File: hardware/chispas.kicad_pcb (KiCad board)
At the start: 2 copper layers, 90 x 60 mm, 41 parts, among them J1 Conn_01x05, J2 Conn_01x04, J3 Conn_01x04, J4 Conn_01x06, J5 Conn_01x02, J6 TRAFO, U1 Heltec_WiFi_LoRa_32_V3, U2 PC817X2CSP9F, U3 PAM8302AASCR

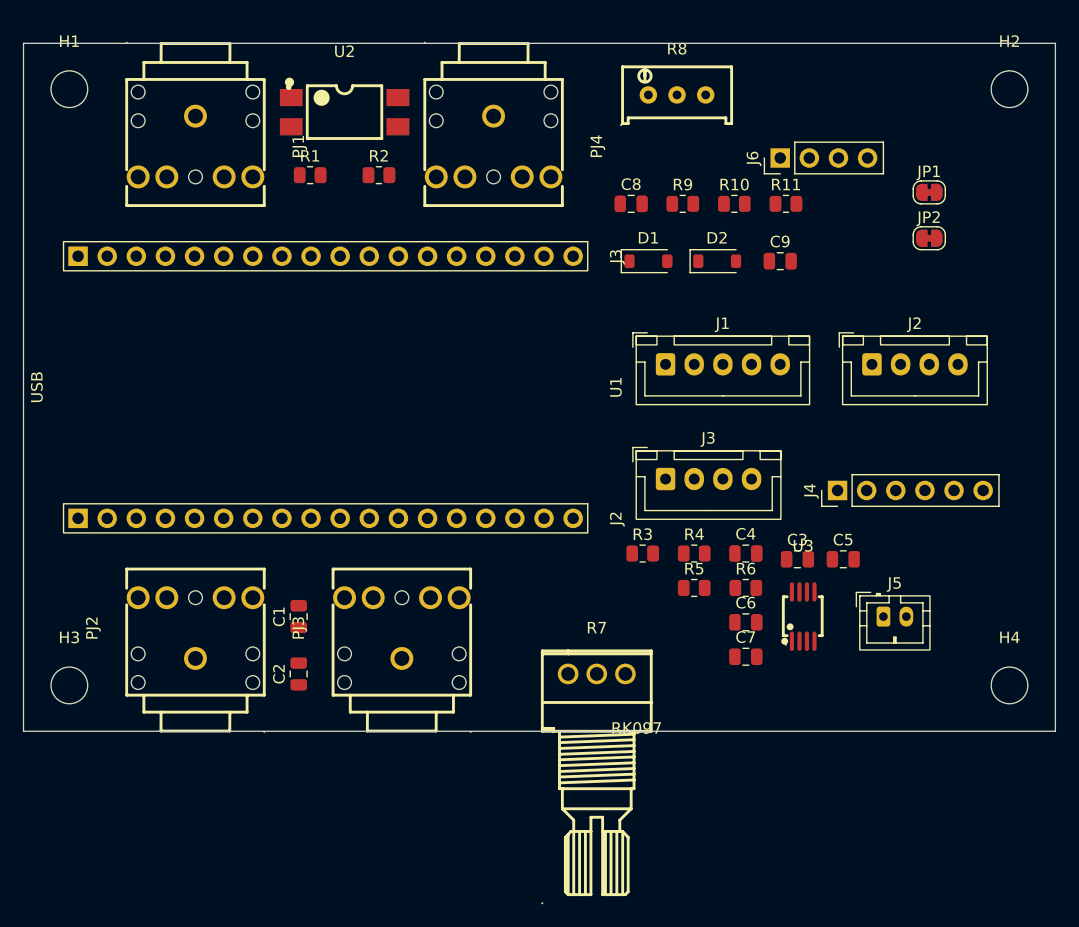
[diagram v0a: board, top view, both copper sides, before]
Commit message: PCB: encoder U4 junto a la Heltec con sus filtros; BME280 y GPS al borde derecho; tira de pines delante
Co-Authored-By: Claude Opus 5.5 <noreply@anthropic.com>
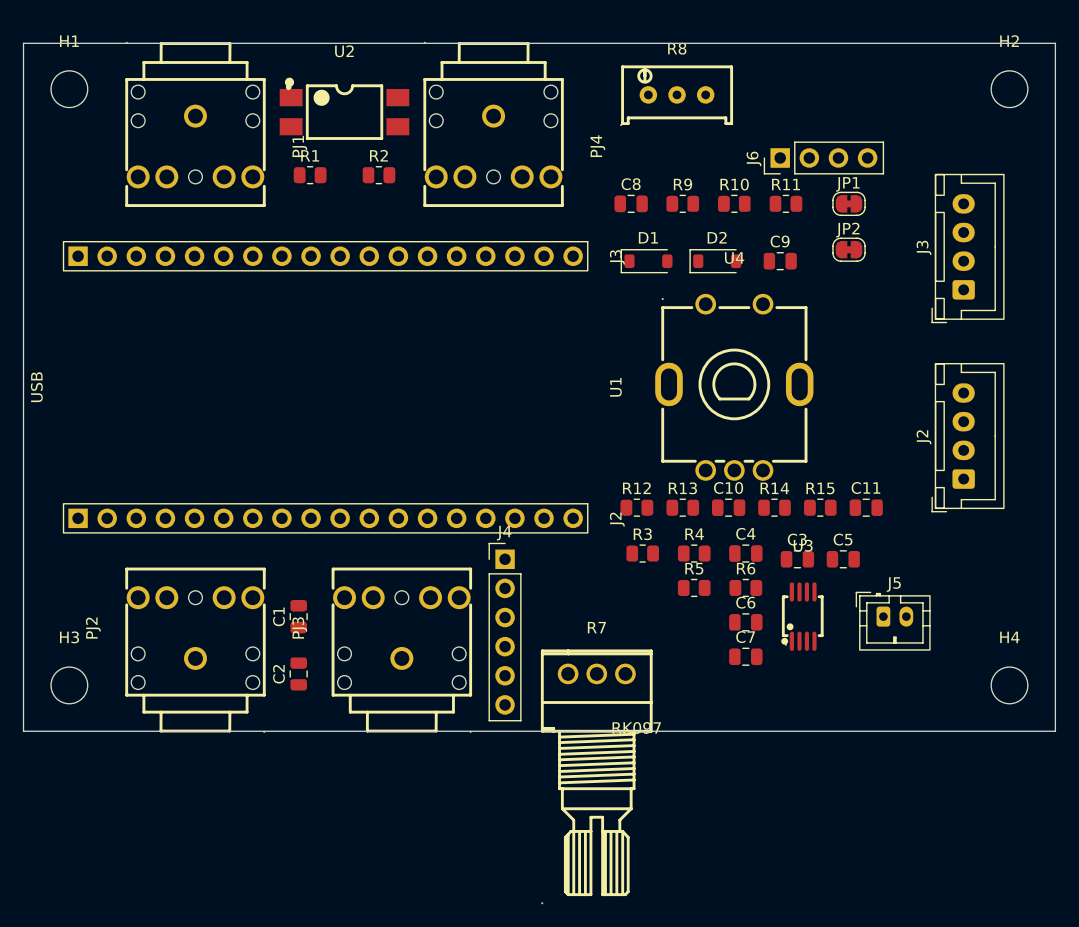
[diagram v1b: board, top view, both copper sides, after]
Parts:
- removed J1: Conn_01x05, Connector_JST:JST_XH_B5B-XH-A_1x05_P2.50mm_Vertical
- added C10: 10n, Capacitor_SMD:C_0805_2012Metric, F.Cu at (161.5, 140.5)
- added C11: 10n, Capacitor_SMD:C_0805_2012Metric, F.Cu at (173.5, 140.5)
- added R12: 10K, Resistor_SMD:R_0805_2012Metric, F.Cu at (153.5, 140.5)
- added R13: 10K, Resistor_SMD:R_0805_2012Metric, F.Cu at (157.5, 140.5)
- added R14: 10K, Resistor_SMD:R_0805_2012Metric, F.Cu at (165.5, 140.5)
- added R15: 10K, Resistor_SMD:R_0805_2012Metric, F.Cu at (169.5, 140.5)
- added U4: PEC11R-4230F-S0024, chispas:SW-TH_PEC11R-4XXXF-SXXXX, F.Cu at (162.0, 130.0)
- moved J3 30.8 mm to (182.0, 121.5), turned to 90 degrees
- moved J4 29.6 mm to (142.0, 145.0), turned to 0 degrees
- moved J2 12.8 mm to (182.0, 138.0), turned to 90 degrees
- moved JP1 7.07 mm to (172.0, 114.0)
- moved JP2 7.07 mm to (172.0, 118.0)

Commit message: PCB: jacks con el cañon asomando 1,65 mm; NOTAS: encoder en placa y requisitos de la caja
Co-Authored-By: Claude Opus 5.5 <noreply@anthropic.com>
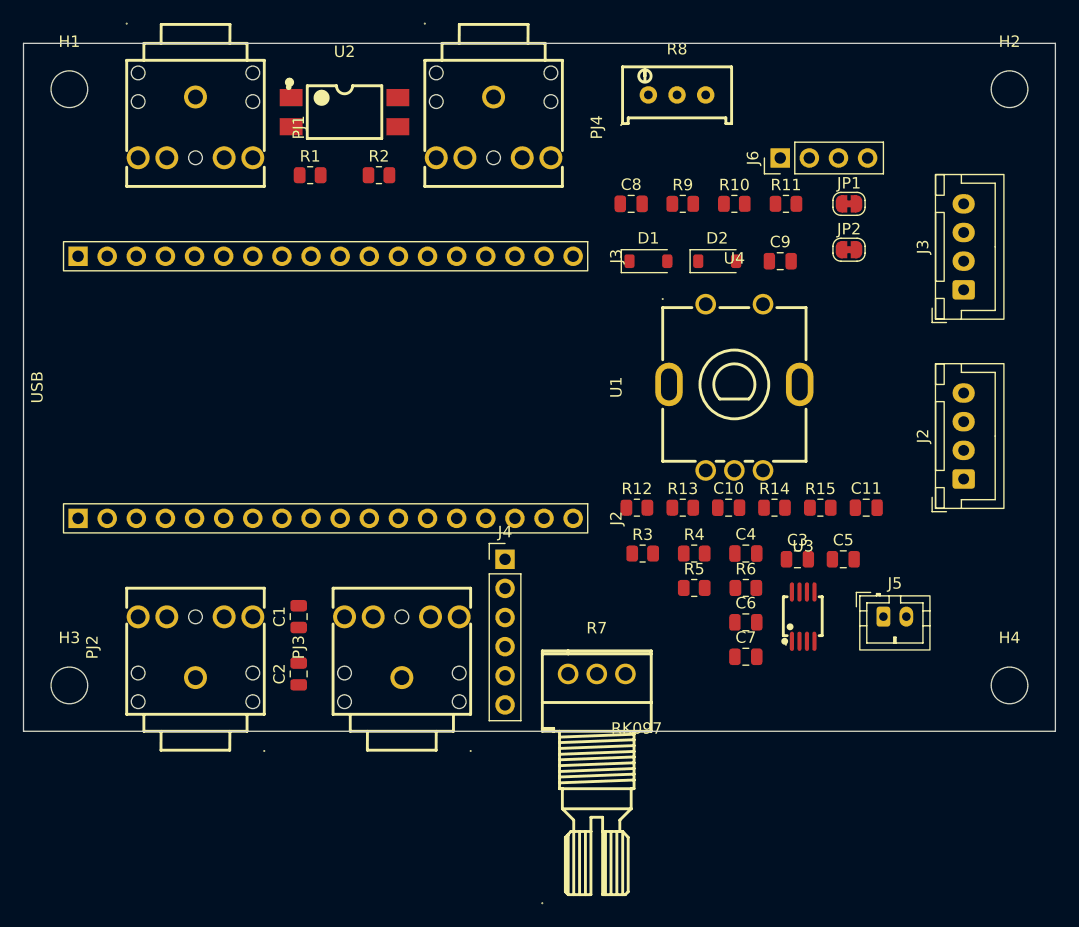
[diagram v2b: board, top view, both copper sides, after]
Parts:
- moved PJ1 1.67 mm to (115.0, 107.3)
- moved PJ4 1.67 mm to (141.0, 107.3)
- moved PJ2 1.67 mm to (115.0, 152.7)
- moved PJ3 1.67 mm to (133.0, 152.7)
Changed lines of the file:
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@@
 	(footprint "chispas:AUDIO-TH_PJ-307"
 		(layer "F.Cu")
-		(at 133 151 90)
+		(at 133 152.67 90)
 		(property "Reference" "PJ3"
 			(at 0 -9 90)
@@
 	(footprint "chispas:AUDIO-TH_PJ-307"
 		(layer "F.Cu")
-		(at 115 109 -90)
+		(at 115 107.33 -90)
 		(property "Reference" "PJ1"
 			(at 0 -9 270)
@@
 	(footprint "chispas:AUDIO-TH_PJ-307"
 		(layer "F.Cu")
-		(at 141 109 -90)
+		(at 141 107.33 -90)
 		(property "Reference" "PJ4"
 			(at 0 -9 270)
@@
 	(footprint "chispas:AUDIO-TH_PJ-307"
 		(layer "F.Cu")
-		(at 115 151 90)
+		(at 115 152.67 90)
 		(property "Reference" "PJ2"
 			(at 0 -9 90)

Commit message: PCB: placa rutada con Freerouting, planos de masa en las dos caras, 116 vias de cosido y zona aislada del KEY (DRC: 0 sin conectar, solo serigrafia)
Co-Authored-By: Claude Opus 5.5 <noreply@anthropic.com>
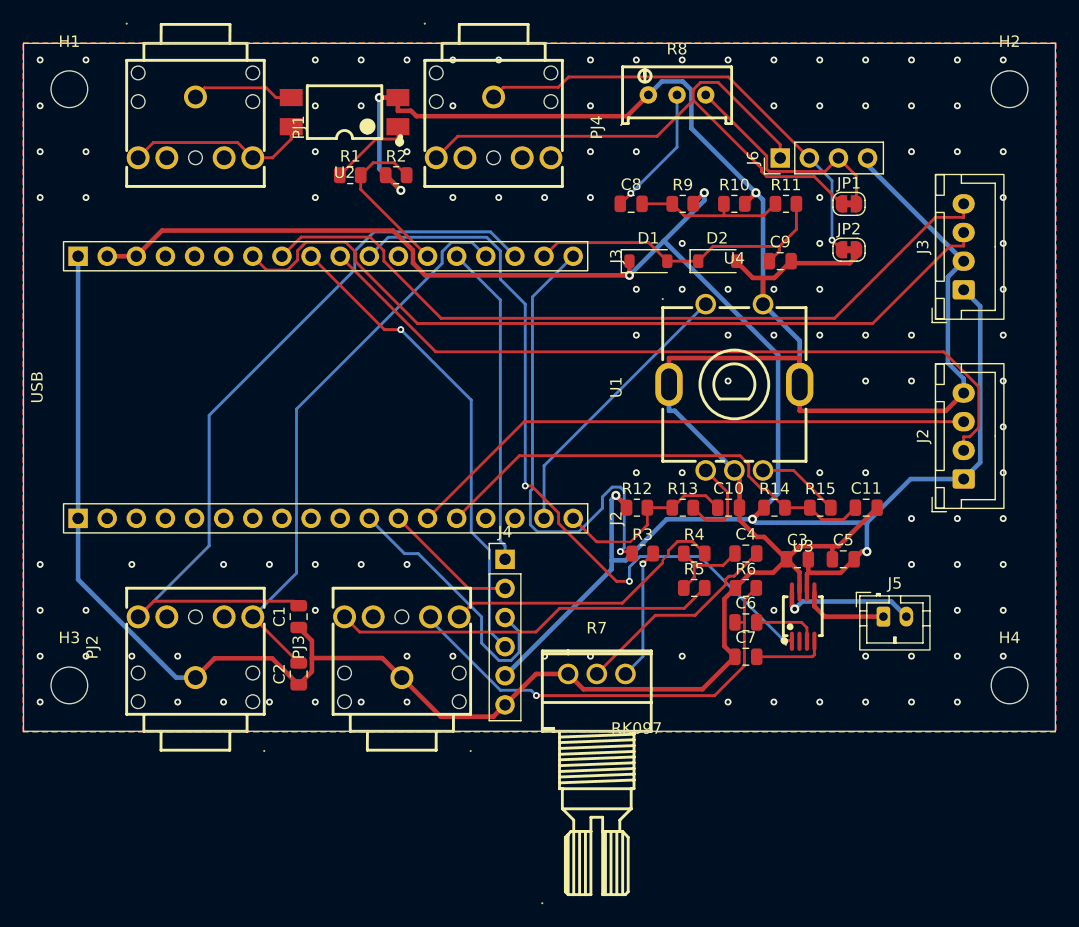
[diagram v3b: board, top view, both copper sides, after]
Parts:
- moved R1 3.50 mm to (128.5, 111.5)
- moved R2 1.50 mm to (132.5, 111.5)
- turned U2 to 180 degrees
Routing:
- net GND: track 0.00 -> 292.6 mm, vias 0 -> 119
- net +3.3V: track 0.00 -> 176.1 mm, vias 0 -> 5
- net /SCL: track 0.00 -> 71.4 mm
- net /DAH: track 0.00 -> 70.0 mm
- net /SDA: track 0.00 -> 68.4 mm
- net /GPS_RX: track 0.00 -> 66.8 mm
- net /AMP_SD: track 0.00 -> 65.9 mm, vias 0 -> 3
- net /TJ: track 0.00 -> 53.5 mm
- net /GPS_TX: track 0.00 -> 50.3 mm
- net /DIT: track 0.00 -> 49.0 mm
- net /TONO: track 0.00 -> 42.3 mm, vias 0 -> 1
- net /GPIO40: track 0.00 -> 41.9 mm, vias 0 -> 1
- net /ENC_DT: track 0.00 -> 40.4 mm
- net /SJ: track 0.00 -> 40.4 mm, vias 0 -> 1
- net /TN: track 0.00 -> 39.5 mm, vias 0 -> 1
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- added copper zone on B.Cu, net GND
- added copper zone on F.Cu, net GND

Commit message: PCB: serigrafia (nombres de conectores, nota del trafo, AUX; datos, licencia y JLCJLCJLCJLC por detras) con serigrafia.py
Co-Authored-By: Claude Opus 5.5 <noreply@anthropic.com>
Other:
- board text added: "ALTAVOZ"
- board text added: "AURIC."
- board text added: "AUX"
- board text added: "BME280"
- board text added: "CHISPAS · EA4ILN"
- board text added: "DECOD"
- board text added: "GPS"
- board text added: "Hardware: CC BY-NC-SA 4.0"
- board text added: "JLCJLCJLCJLC"
- board text added: "KEY"
- board text added: "PALAS"
- board text added: "PCB v1.0 (2026)"
- board text added: "TRAFO"
- board text added: "VOL"
- board text added: "cortar=trafo"
- board text added: "github.com/ea4iln-debug/CHISPAS-EA4ILN"

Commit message: PCB: serigrafia KEY -> PTT y PALAS -> KEYER
Co-Authored-By: Claude Opus 5.5 <noreply@anthropic.com>
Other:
- board text added: "KEYER"
- board text added: "PTT"
- board text removed: "KEY"
- board text removed: "PALAS"
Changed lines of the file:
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@@
 		)
 	)
-	(gr_text "KEY"
+	(gr_text "PTT"
 		(at 115 114.6 0)
 		(layer "F.SilkS")
@@
 		)
 	)
-	(gr_text "PALAS"
+	(gr_text "KEYER"
 		(at 115 145.4 0)
 		(layer "F.SilkS")

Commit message: PCB: serigrafia PTT -> KEY OUT
Co-Authored-By: Claude Opus 5.5 <noreply@anthropic.com>
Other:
- board text added: "KEY OUT"
- board text removed: "PTT"
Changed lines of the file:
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@@
 		)
 	)
-	(gr_text "PTT"
+	(gr_text "KEY OUT"
 		(at 115 114.6 0)
 		(layer "F.SilkS")

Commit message: PCB: serigrafia PTT -> KEY OUT y KEYER -> KEY IN
Co-Authored-By: Claude Opus 5.5 <noreply@anthropic.com>
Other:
- board text added: "KEY IN"
- board text removed: "KEYER"
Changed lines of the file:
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@@
 		)
 	)
-	(gr_text "KEYER"
+	(gr_text "KEY IN"
 		(at 115 145.4 0)
 		(layer "F.SilkS")
